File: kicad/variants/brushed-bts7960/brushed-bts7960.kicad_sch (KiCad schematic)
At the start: 69 parts, among them IC1 rp2040_RP2040_breakout_swd, J1 HDR-M-2.54_1x3, J2 HDR-M-2.54_1x4, J3 HDR-M-2.54_1x4, J4 HDR-M-2.54_1x4, U1 SN74AHC244DW, U2 BTN7970, U3 BTN7970, U4 BTN7970, U5 BTN7970, U6 BMI160, U7 SPX3819M5-L-3-3/TR

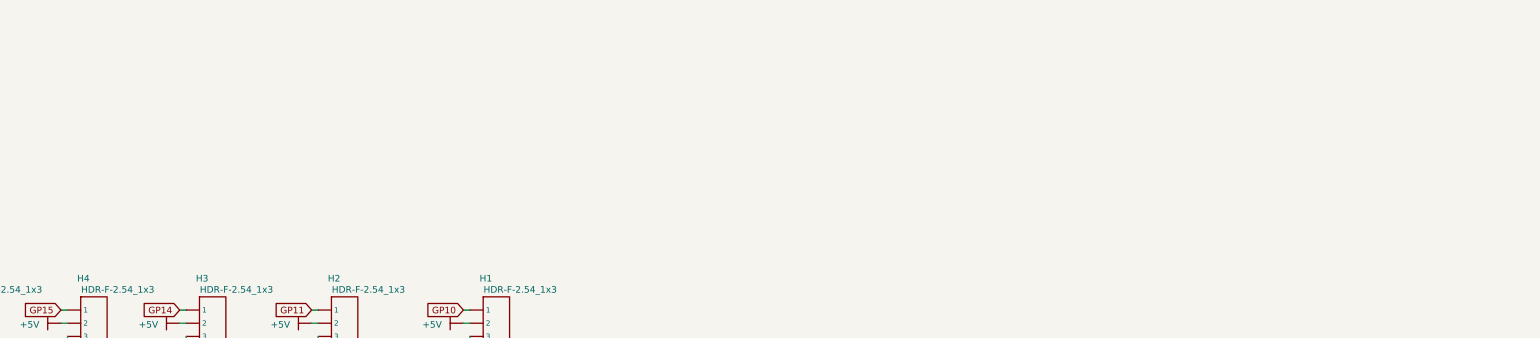
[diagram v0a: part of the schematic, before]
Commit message: feat(kicad): антиспарк-выключатель шины 24 В (LTC7004 + 2× N-MOSFET, лист 2)
Добавлен отдельный лист antispark.kicad_sch: драйвер верхнего плеча LTC7004,
два ключа IPB020N10N5 на плюсе, RC-рампа затвора (~0.45 А, 24 В за ~0.13 с),
78L12 для VCC драйвера с защитой D3/R33, делитель INP, выключатель на J5
(перемычка/тумблер, ~1 мА) и LED-индикатор VIN. Клемма батареи становится
BAT+, после ключа — прежняя шина VIN; PWR_FLAG на GND закрывает ошибку ERC.

Символы LTC7004 и Q_NMOS_GDS дописаны в biba.kicad_sym. Обновлены README
варианта (статус, блок-схема, силовые цепи, BOM, ERC), README kicad/ и
common/README.md (лист 2, ручные символы после импорта), analysis/
M1-driver-failure.md (третий TVS на VIN — теперь D6). На плату блок не
перенесён — отдельный шаг в «Дальнейших шагах».
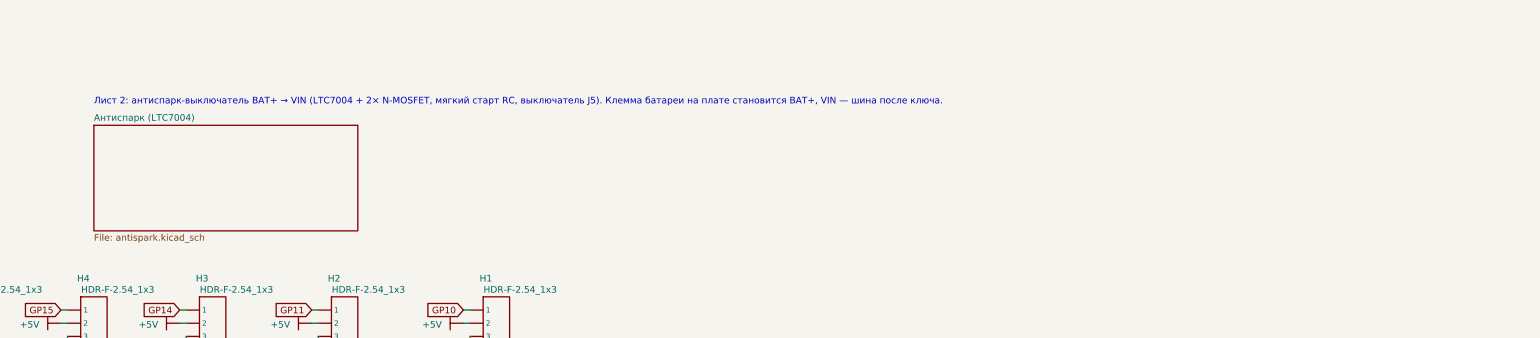
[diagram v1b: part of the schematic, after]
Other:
- added sheet Антиспарк (LTC7004) (antispark.kicad_sch)
- note added: "Лист 2: антиспарк-выключатель BAT+ → VIN (LTC7004 + 2× N-MOSFET, мягкий старт RC, выключатель J5). Клемма батареи на плате становится BAT+, VIN — шина после ключа."
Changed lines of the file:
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@@
   )
   (no_connect (at 257.81 247.65))
+  (text "Лист 2: антиспарк-выключатель BAT+ → VIN (LTC7004 + 2× N-MOSFET, мягкий старт RC, выключатель J5). Клемма батареи на плате становится BAT+, VIN — шина после ключа."
+    (at 304.8 168.91 0)
+    (effects
+      (font
+        (size 1.27 1.27))
+      (justify left bottom))
+)
+  (sheet
+    (at 304.8 172.72)
+    (size 50.8 20.32)
+    (fields_autoplaced yes)
+    (stroke
+      (width 0.1524)
+      (type solid))
+    (fill
+      (color 0 0 0 0.0000))
+    (property "Sheetname" "Антиспарк (LTC7004)"
+      (at 304.8 172.0 0)
+      (effects
+        (font
+          (size 1.27 1.27))
+        (justify left bottom)))
+    (property "Sheetfile" "antispark.kicad_sch"
+      (at 304.8 193.6 0)
+      (effects
+        (font
+          (size 1.27 1.27))
+        (justify left top)))
+    (instances
+      (project "brushed-bts7960"
+        (path "/5d1025ef-bd26-5426-bb12-5355817dfc1c"
+          (page "2")))))
   (sheet_instances
     (path "/" (page "1"))
